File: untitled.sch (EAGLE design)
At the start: 15 parts, among them IC1 ACS758LCB-050B-PFF-T, IC2 LM2936DT-3.3

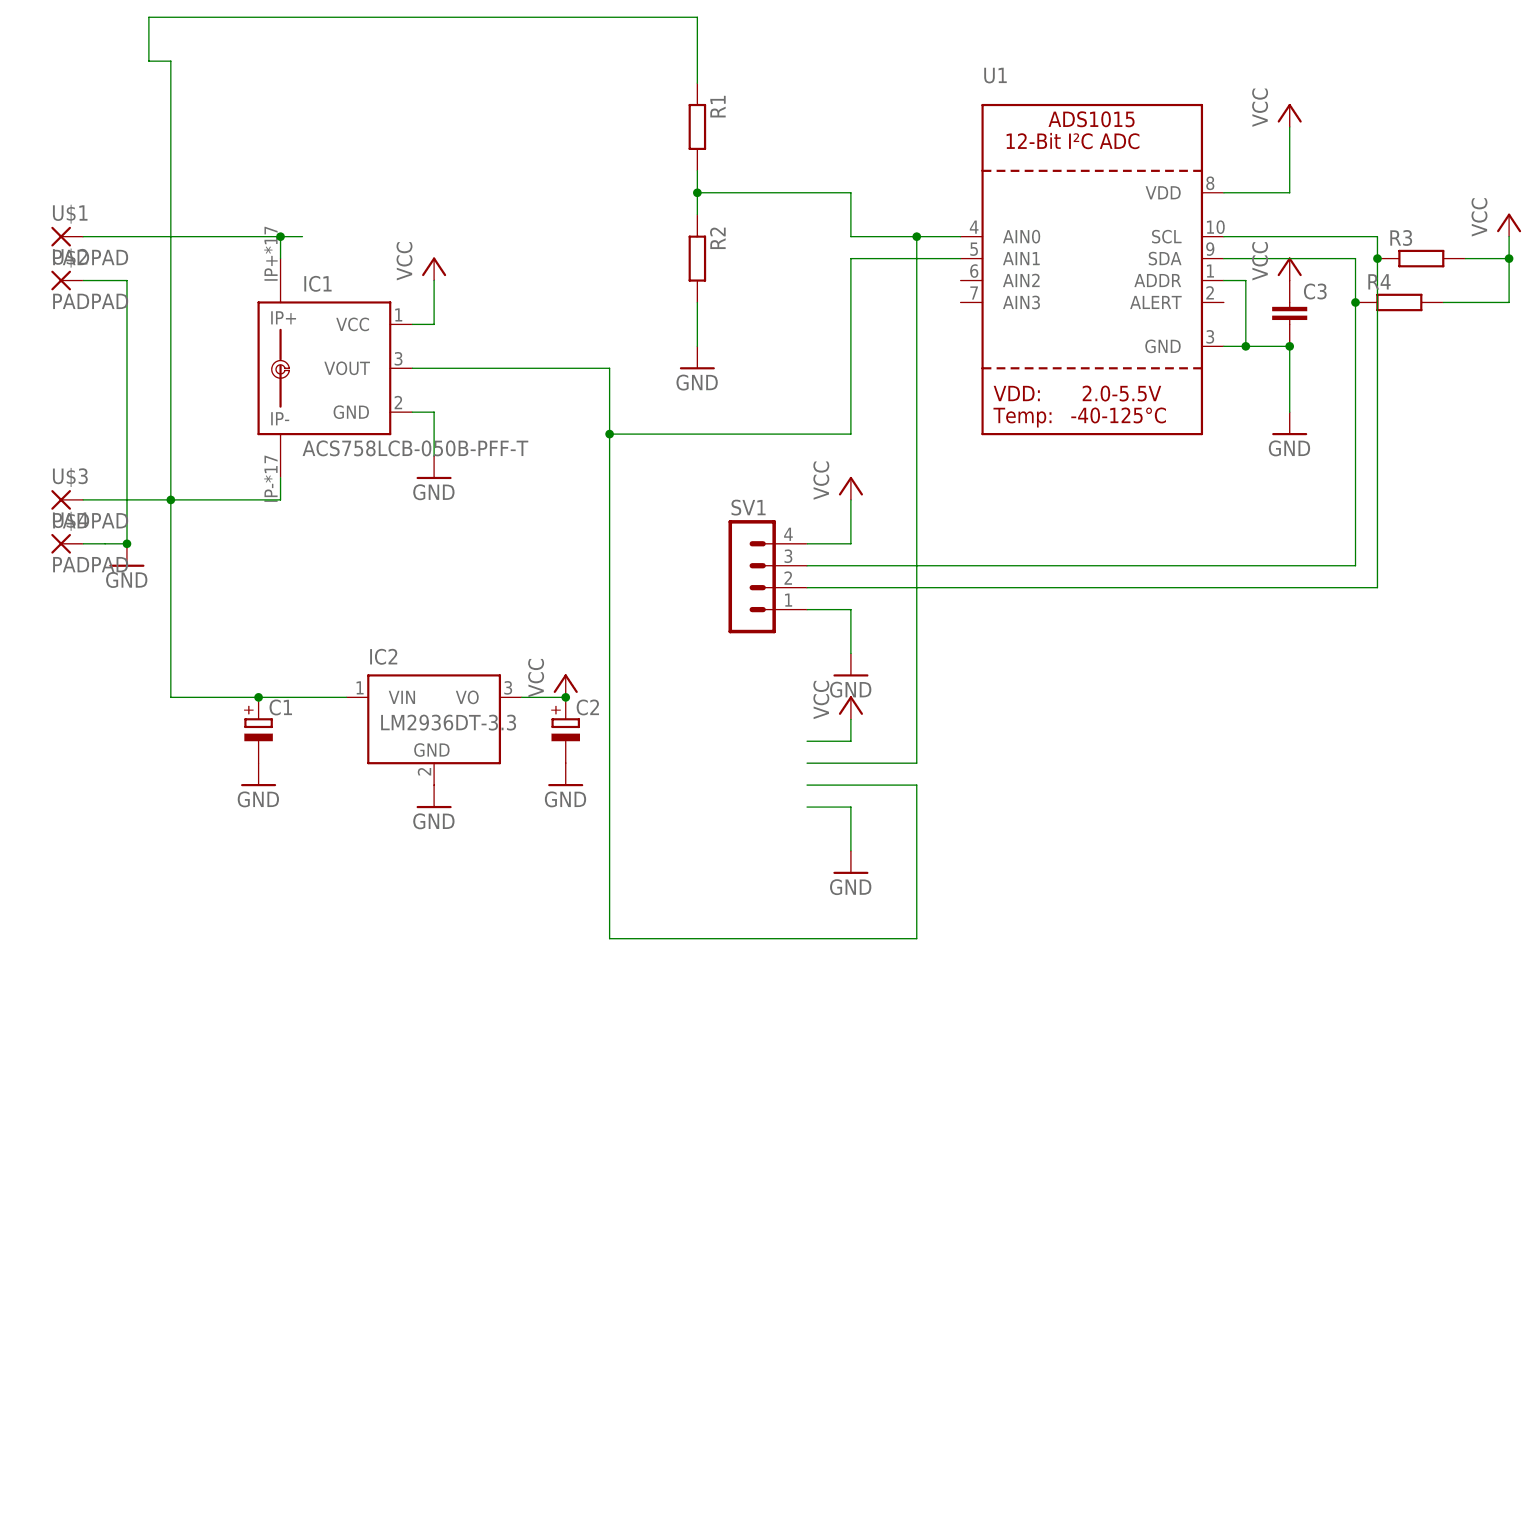
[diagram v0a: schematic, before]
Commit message: Add new schematic for new dc dc converter
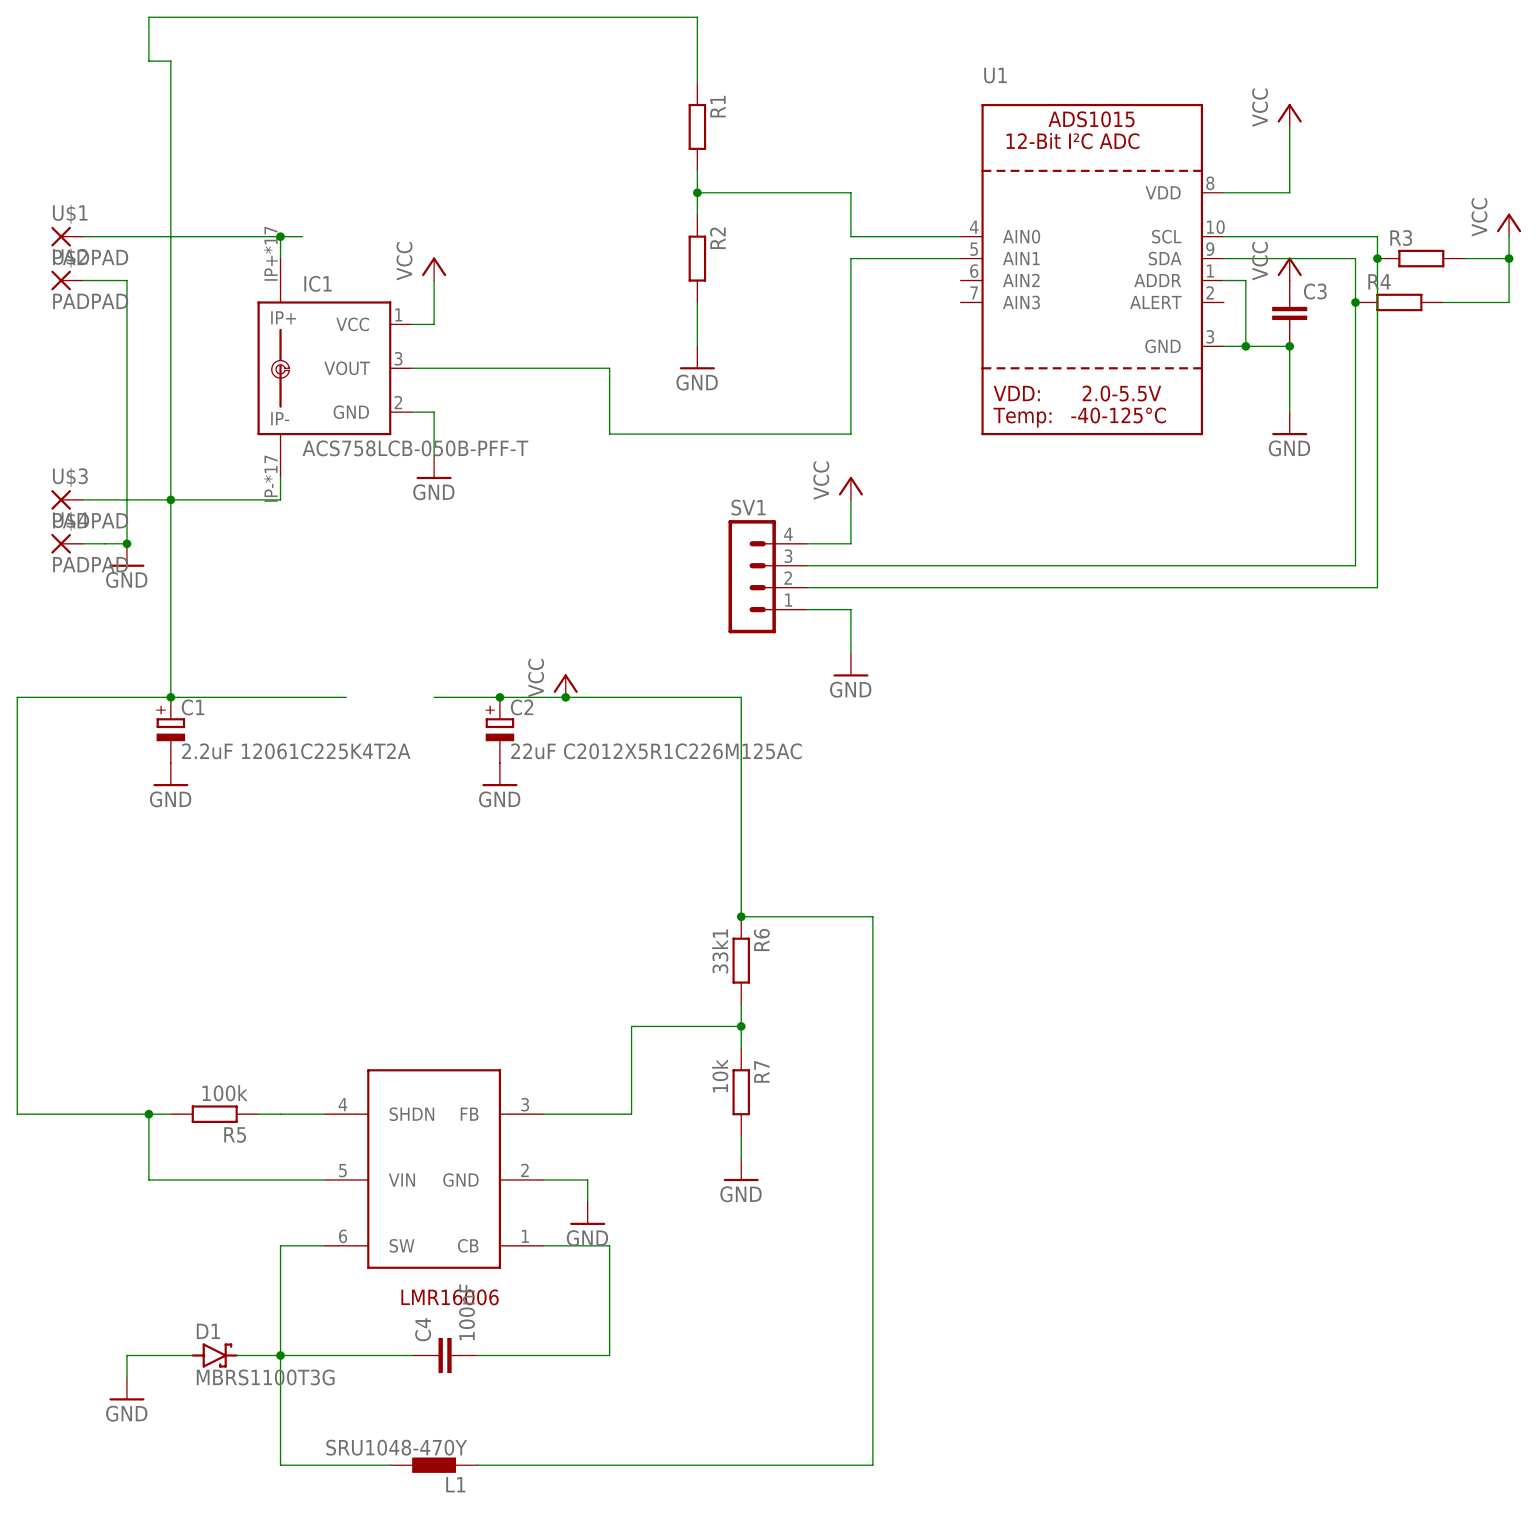
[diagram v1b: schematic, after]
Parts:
- removed IC2: LM2936DT-3.3, national-semiconductor:LM2936DT-3.3
- added C4: 100nF, rcl:C-EUC0805
- added D1: MBRS1100T3G, diode:BAT60J
- added L1: SRU1048-470Y, inductors:DR1030
- added R5: 100k, rcl:R-EU_M0805
- added R6: 33k1, rcl:R-EU_M0805
- added R7: 10k, rcl:R-EU_M0805
- added U$5: LMR16006, texas:LMR16006
- C1: value (none) -> 2.2uF 12061C225K4T2A; device rcl:CPOL-EU153CLV-0505 -> rcl:CPOL-EUA/3216-18R
- C2: value (none) -> 22uF C2012X5R1C226M125AC; device rcl:CPOL-EU153CLV-0505 -> rcl:CPOL-EUR/2012-12R
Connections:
- new net N$10: C4.2, U$5.CB
- new net N$11: R6.2, R7.1, U$5.FB
- new net N$3: R5.1, U$5.SHDN
- new net N$9: C4.1, D1.C, L1.2, U$5.SW
- net GND: now also D1.A, R7.2, U$5.GND; no longer IC2.GND
- net N$4: now also R5.2, U$5.VIN; no longer IC2.VIN
- net VCC: now also L1.1, R6.1; no longer IC2.VO
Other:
- moved on the sheet: C1, C2

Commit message: Update board layout
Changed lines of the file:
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@@
 <pinref part="P+6" gate="VCC" pin="VCC"/>
 <wire x1="53.34" y1="38.1" x2="45.72" y2="38.1" width="0.1524" layer="91"/>
-<wire x1="45.72" y1="38.1" x2="38.1" y2="38.1" width="0.1524" layer="91"/>
 <pinref part="C2" gate="G$1" pin="+"/>
-<junction x="45.72" y="38.1"/>
 <pinref part="L1" gate="G$1" pin="1"/>
 <wire x1="43.18" y1="-50.8" x2="88.9" y2="-50.8" width="0.1524" layer="91"/>
@@
 <wire x1="5.08" y1="111.76" x2="5.08" y2="116.84" width="0.1524" layer="91"/>
 <wire x1="7.62" y1="60.96" x2="7.62" y2="38.1" width="0.1524" layer="91"/>
-<wire x1="7.62" y1="38.1" x2="27.94" y2="38.1" width="0.1524" layer="91"/>
 <pinref part="U$3" gate="G$1" pin="P"/>
 <pinref part="C1" gate="G$1" pin="+"/>

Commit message: Update components
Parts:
- removed C2: 22uF C2012X5R1C226M125AC, rcl:CPOL-EUR/2012-12R
- removed L1: SRU1048-470Y, inductors:DR1030
- added C5: 22uF 100V, rcl:CPOL-EU150CLZ-0810
- added L2: 100uH, inductors:DR125
- C1: value 2.2uF 12061C225K4T2A -> 47uF 16v; device rcl:CPOL-EUA/3216-18R -> rcl:CPOL-EU153CLV-0505
- C3: value (none) -> 100nF
- R3, R4: value (none) -> 10k
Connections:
- net GND: now also C5.-; no longer C2.-
- net N$4: now also C5.+; no longer C1.+
- net N$9: now also L2.1; no longer L1.2
- net VCC: now also C1.+, L2.2; no longer C2.+, L1.1
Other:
- moved on the sheet: C1

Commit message: Update capacitors
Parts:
- removed C1: 47uF 16v, rcl:CPOL-EU153CLV-0505
- removed C5: 22uF 100V, rcl:CPOL-EU150CLZ-0810
- added C2: 2.2uF 100V, rcl:CPOL-EUA/3216-18R
- added C6: 22uF 25V, rcl:CPOL-EUR/2012-12R
- R1, R2, R3, R4: device rcl:R-EU_R1206 -> rcl:R-EU_R0805
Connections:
- net GND: now also C2.-, C6.-; no longer C1.-, C5.-
- net N$4: now also C2.+; no longer C5.+
- net VCC: now also C6.+; no longer C1.+
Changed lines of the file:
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@@
 <grid distance="0.1" unitdist="inch" unit="inch" style="lines" multiple="1" display="no" altdistance="0.01" altunitdist="inch" altunit="inch"/>
 <layers>
-<layer number="1" name="Top" color="4" fill="1" visible="no" active="no"/>
-<layer number="16" name="Bottom" color="1" fill="1" visible="no" active="no"/>
-<layer number="17" name="Pads" color="2" fill="1" visible="no" active="no"/>
-<layer number="18" name="Vias" color="2" fill="1" visible="no" active="no"/>
-<layer number="19" name="Unrouted" color="6" fill="1" visible="no" active="no"/>
-<layer number="20" name="Dimension" color="24" fill="1" visible="no" active="no"/>
-<layer number="21" name="tPlace" color="7" fill="1" visible="no" active="no"/>
-<layer number="22" name="bPlace" color="7" fill="1" visible="no" active="no"/>
-<layer number="23" name="tOrigins" color="15" fill="1" visible="no" active="no"/>
-<layer number="24" name="bOrigins" color="15" fill="1" visible="no" active="no"/>
-<layer number="25" name="tNames" color="7" fill="1" visible="no" active="no"/>
-<layer number="26" name="bNames" color="7" fill="1" visible="no" active="no"/>
-<layer number="27" name="tValues" color="7" fill="1" visible="no" active="no"/>
-<layer number="28" name="bValues" color="7" fill="1" visible="no" active="no"/>
+<layer number="1" name="Top" color="4" fill="1" visible="yes" active="no"/>
+<layer number="16" name="Bottom" color="1" fill="1" visible="yes" active="no"/>
+<layer number="17" name="Pads" color="2" fill="1" visible="yes" active="no"/>
+<layer number="18" name="Vias" color="2" fill="1" visible="yes" active="no"/>
+<layer number="19" name="Unrouted" color="6" fill="1" visible="yes" active="no"/>
+<layer number="20" name="Dimension" color="24" fill="1" visible="yes" active="no"/>
+<layer number="21" name="tPlace" color="7" fill="1" visible="yes" active="no"/>
+<layer number="22" name="bPlace" color="7" fill="1" visible="yes" active="no"/>
+<layer number="23" name="tOrigins" color="15" fill="1" visible="yes" active="no"/>
+<layer number="24" name="bOrigins" color="15" fill="1" visible="yes" active="no"/>
+<layer number="25" name="tNames" color="7" fill="1" visible="yes" active="no"/>
+<layer number="26" name="bNames" color="7" fill="1" visible="yes" active="no"/>
+<layer number="27" name="tValues" color="7" fill="1" visible="yes" active="no"/>
+<layer number="28" name="bValues" color="7" fill="1" visible="yes" active="no"/>
 <layer number="29" name="tStop" color="7" fill="3" visible="no" active="no"/>
 <layer number="30" name="bStop" color="7" fill="6" visible="no" active="no"/>
@@
 <layer number="35" name="tGlue" color="7" fill="4" visible="no" active="no"/>
 <layer number="36" name="bGlue" color="7" fill="5" visible="no" active="no"/>
-<layer number="37" name="tTest" color="7" fill="1" visible="no" active="no"/>
-<layer number="38" name="bTest" color="7" fill="1" visible="no" active="no"/>
+<layer number="37" name="tTest" color="7" fill="1" visible="yes" active="no"/>
+<layer number="38" name="bTest" color="7" fill="1" visible="yes" active="no"/>
 <layer number="39" name="tKeepout" color="4" fill="11" visible="no" active="no"/>
 <layer number="40" name="bKeepout" color="1" fill="11" visible="no" active="no"/>
@@
 <layer number="44" name="Drills" color="7" fill="1" visible="no" active="no"/>
 <layer number="45" name="Holes" color="7" fill="1" visible="no" active="no"/>
-<layer number="46" name="Milling" color="3" fill="1" visible="no" active="no"/>
-<layer number="47" name="Measures" color="7" fill="1" visible="no" active="no"/>
-<layer number="48" name="Document" color="7" fill="1" visible="no" active="no"/>
-<layer number="49" name="Reference" color="7" fill="1" visible="no" active="no"/>
-<layer number="50" name="dxf" color="7" fill="1" visible="no" active="no"/>
-<layer number="51" name="tDocu" color="7" fill="1" visible="no" active="no"/>
-<layer number="52" name="bDocu" color="7" fill="1" visible="no" active="no"/>
-<layer number="53" name="tGND_GNDA" color="7" fill="9" visible="no" active="no"/>
-<layer number="54" name="bGND_GNDA" color="1" fill="9" visible="no" active="no"/>
-<layer number="56" name="wert" color="7" fill="1" visible="no" active="no"/>
-<layer number="57" name="tCAD" color="7" fill="1" visible="no" active="no"/>
+<layer number="46" name="Milling" color="3" fill="1" visible="yes" active="no"/>
+<layer number="47" name="Measures" color="7" fill="1" visible="yes" active="no"/>
+<layer number="48" name="Document" color="7" fill="1" visible="yes" active="no"/>
+<layer number="49" name="Reference" color="7" fill="1" visible="yes" active="no"/>
+<layer number="50" name="dxf" color="7" fill="1" visible="yes" active="no"/>
+<layer number="51" name="tDocu" color="7" fill="1" visible="yes" active="no"/>
+<layer number="52" name="bDocu" color="7" fill="1" visible="yes" active="no"/>
+<layer number="53" name="tGND_GNDA" color="7" fill="9" visible="yes" active="no"/>
+<layer number="54" name="bGND_GNDA" color="1" fill="9" visible="yes" active="no"/>
+<layer number="56" name="wert" color="7" fill="1" visible="yes" active="no"/>
+<layer number="57" name="tCAD" color="7" fill="1" visible="yes" active="no"/>
 <layer number="88" name="SimResults" color="9" fill="1" visible="yes" active="yes"/>
 <layer number="89" name="SimProbes" color="9" fill="1" visible="yes" active="yes"/>
@@
 <part name="SV1" library="con-lstb" library_urn="urn:adsk.eagle:library:162" deviceset="MA04-1" device="" package3d_urn="urn:adsk.eagle:package:8337/1"/>
 <part name="U1" library="microbuilder" deviceset="ADC_ADS1015" device=""/>
-<part name="R1" library="rcl" library_urn="urn:adsk.eagle:library:334" deviceset="R-EU_" device="R1206" package3d_urn="urn:adsk.eagle:package:23540/2"/>
-<part name="R2" library="rcl" library_urn="urn:adsk.eagle:library:334" deviceset="R-EU_" device="R1206" package3d_urn="urn:adsk.eagle:package:23540/2"/>
+<part name="R1" library="rcl" library_urn="urn:adsk.eagle:library:334" deviceset="R-EU_" device="R0805" package3d_urn="urn:adsk.eagle:package:23553/2"/>
+<part name="R2" library="rcl" library_urn="urn:adsk.eagle:library:334" deviceset="R-EU_" device="R0805" package3d_urn="urn:adsk.eagle:package:23553/2"/>
 <part name="GND2" library="supply1" library_urn="urn:adsk.eagle:library:371" deviceset="GND" device=""/>
 <part name="GND3" library="supply1" library_urn="urn:adsk.eagle:library:371" deviceset="GND" device=""/>
@@
 <part name="P+2" library="supply1" library_urn="urn:adsk.eagle:library:371" deviceset="VCC" device=""/>
 <part name="P+4" library="supply1" library_urn="urn:adsk.eagle:library:371" deviceset="VCC" device=""/>
-<part name="R3" library="rcl" library_urn="urn:adsk.eagle:library:334" deviceset="R-EU_" device="R1206" package3d_urn="urn:adsk.eagle:package:23540/2" value="10k"/>
-<part name="R4" library="rcl" library_urn="urn:adsk.eagle:library:334" deviceset="R-EU_" device="R1206" package3d_urn="urn:adsk.eagle:package:23540/2" value="10k"/>
+<part name="R3" library="rcl" library_urn="urn:adsk.eagle:library:334" deviceset="R-EU_" device="R0805" package3d_urn="urn:adsk.eagle:package:23553/2" value="10k"/>
+<part name="R4" library="rcl" library_urn="urn:adsk.eagle:library:334" deviceset="R-EU_" device="R0805" package3d_urn="urn:adsk.eagle:package:23553/2" value="10k"/>
 <part name="P+5" library="supply1" library_urn="urn:adsk.eagle:library:371" deviceset="VCC" device=""/>
 <part name="GND6" library="supply1" library_urn="urn:adsk.eagle:library:371" deviceset="GND" device=""/>
@@
 <part name="GND10" library="supply1" library_urn="urn:adsk.eagle:library:371" deviceset="GND" device=""/>
 <part name="L2" library="inductors" library_urn="urn:adsk.eagle:library:243" deviceset="DR125" device="" package3d_urn="urn:adsk.eagle:package:15121/1" value="100uH "/>
-<part name="C5" library="rcl" library_urn="urn:adsk.eagle:library:334" deviceset="CPOL-EU" device="150CLZ-0810" package3d_urn="urn:adsk.eagle:package:23394/2" value="22uF 100V"/>
-<part name="C1" library="rcl" library_urn="urn:adsk.eagle:library:334" deviceset="CPOL-EU" device="153CLV-0505" package3d_urn="urn:adsk.eagle:package:23402/2" value="47uF 16v"/>
+<part name="C2" library="rcl" library_urn="urn:adsk.eagle:library:334" deviceset="CPOL-EU" device="A/3216-18R" package3d_urn="urn:adsk.eagle:package:23410/2" value="2.2uF 100V"/>
+<part name="C6" library="rcl" library_urn="urn:adsk.eagle:library:334" deviceset="CPOL-EU" device="R/2012-12R" package3d_urn="urn:adsk.eagle:package:23426/2" value="22uF 25V"/>
 </parts>
 <sheets>
@@
 <attribute name="VALUE" x="39.243" y="-56.388" size="1.778" layer="96"/>
 </instance>
-<instance part="C5" gate="G$1" x="7.62" y="35.56" smashed="yes">
+<instance part="C2" gate="G$1" x="7.62" y="35.56" smashed="yes">
 <attribute name="NAME" x="8.763" y="36.0426" size="1.778" layer="95"/>
 <attribute name="VALUE" x="8.763" y="30.9626" size="1.778" layer="96"/>
 </instance>
-<instance part="C1" gate="G$1" x="45.72" y="35.56" smashed="yes">
+<instance part="C6" gate="G$1" x="45.72" y="35.56" smashed="yes">
 <attribute name="NAME" x="46.863" y="36.0426" size="1.778" layer="95"/>
 <attribute name="VALUE" x="46.863" y="30.9626" size="1.778" layer="96"/>
@@
 <junction x="53.34" y="38.1"/>
 <pinref part="L2" gate="G$1" pin="2"/>
-<pinref part="C1" gate="G$1" pin="+"/>
+<pinref part="C6" gate="G$1" pin="+"/>
 </segment>
 <segment>
@@
 <segment>
 <pinref part="GND7" gate="1" pin="GND"/>
-<pinref part="C5" gate="G$1" pin="-"/>
+<pinref part="C2" gate="G$1" pin="-"/>
 </segment>
 <segment>
 <pinref part="GND8" gate="1" pin="GND"/>
-<pinref part="C1" gate="G$1" pin="-"/>
+<pinref part="C6" gate="G$1" pin="-"/>
 </segment>
 </net>
@@
 <wire x1="-10.16" y1="-10.16" x2="5.08" y2="-10.16" width="0.1524" layer="91"/>
 <junction x="5.08" y="-10.16"/>
-<pinref part="C5" gate="G$1" pin="+"/>
+<pinref part="C2" gate="G$1" pin="+"/>
 <junction x="7.62" y="38.1"/>
 </segment>
